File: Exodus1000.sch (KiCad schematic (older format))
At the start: 3 parts, among them J3 Conn_01x02

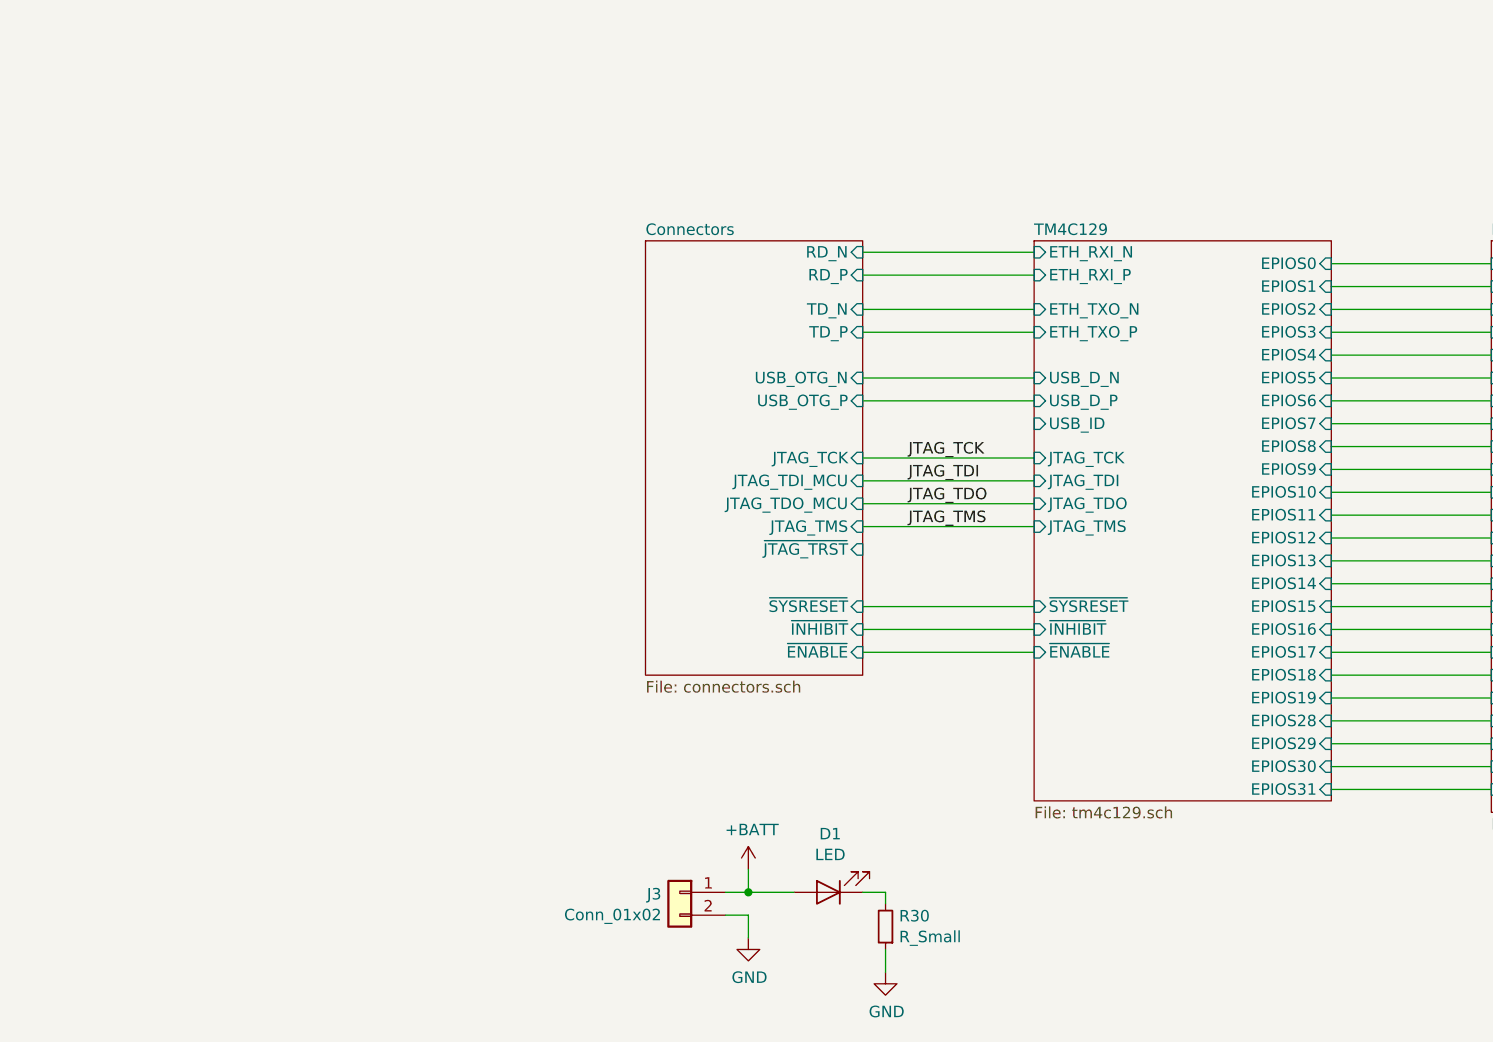
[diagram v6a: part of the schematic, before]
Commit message: layout done sans connector. It's pretty big. Likely going to need to tear some of this up.
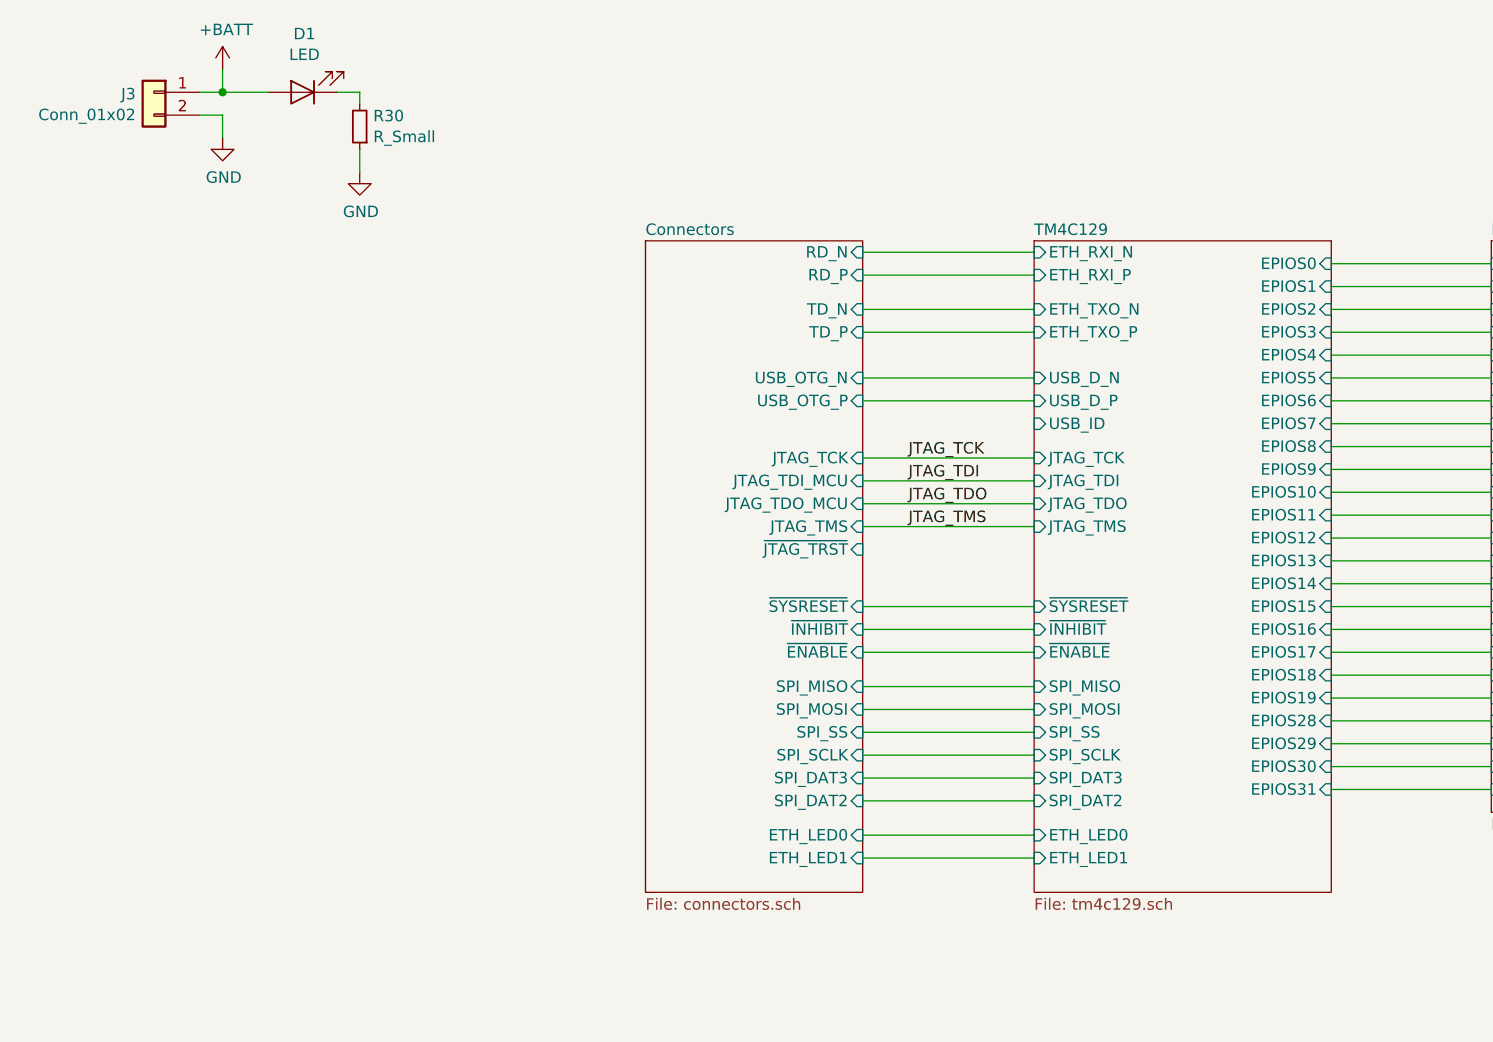
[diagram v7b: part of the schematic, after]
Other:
- moved on the sheet: D1, J3, R30
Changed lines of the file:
@@
 $EndDescr
 $Sheet
-S 5450 2050 1300 2450
+S 5450 2050 1300 2850
 U 5C80AE96
 F0 "TM4C129" 50
@@
 F38 "~INHIBIT" I L 5450 3750 50
 F39 "~SYSRESET" I L 5450 3650 50
+F40 "SPI_MISO" I L 5450 4000 50
+F41 "SPI_MOSI" I L 5450 4100 50
+F42 "SPI_SS" I L 5450 4200 50
+F43 "SPI_SCLK" I L 5450 4300 50
+F44 "SPI_DAT3" I L 5450 4400 50
+F45 "SPI_DAT2" I L 5450 4500 50
+F46 "ETH_LED0" I L 5450 4650 50
+F47 "ETH_LED1" I L 5450 4750 50
 $EndSheet
 $Sheet
-S 3750 2050 950  1900
+S 3750 2050 950  2850
 U 5C8128A2
 F0 "Connectors" 50
@@
 F14 "JTAG_TDI_MCU" I R 4700 3100 50
 F15 "JTAG_TDO_MCU" I R 4700 3200 50
+F16 "SPI_MISO" I R 4700 4000 50
+F17 "SPI_MOSI" I R 4700 4100 50
+F18 "SPI_SS" I R 4700 4200 50
+F19 "SPI_SCLK" I R 4700 4300 50
+F20 "SPI_DAT3" I R 4700 4400 50
+F21 "SPI_DAT2" I R 4700 4500 50
+F22 "ETH_LED0" I R 4700 4650 50
+F23 "ETH_LED1" I R 4700 4750 50
 $EndSheet
 Text Label 4900 3000 0    50   ~ 0
@@
 JTAG_TMS
 Wire Wire Line
-	4100 4900 4200 4900
-Wire Wire Line
-	4200 4900 4200 4800
-Wire Wire Line
-	4100 5000 4200 5000
-Wire Wire Line
-	4200 5000 4200 5100
+	1800 1400 1900 1400
+Wire Wire Line
+	1900 1400 1900 1300
+Wire Wire Line
+	1800 1500 1900 1500
+Wire Wire Line
+	1900 1500 1900 1600
 $Comp
 L power:GND #PWR0149
 U 1 1 5C8F5DB2
-P 4200 5100
-F 0 "#PWR0149" H 4200 4850 50  0001 C CNN
-F 1 "GND" H 4205 4927 50  0000 C CNN
-F 2 "" H 4200 5100 50  0001 C CNN
-F 3 "" H 4200 5100 50  0001 C CNN
-	1    4200 5100
+P 1900 1600
+F 0 "#PWR0149" H 1900 1350 50  0001 C CNN
+F 1 "GND" H 1905 1427 50  0000 C CNN
+F 2 "" H 1900 1600 50  0001 C CNN
+F 3 "" H 1900 1600 50  0001 C CNN
+	1    1900 1600
 	1    0    0    -1
 $EndComp
@@
 L power:+BATT #PWR0150
 U 1 1 5C8F5ED8
-P 4200 4800
-F 0 "#PWR0150" H 4200 4650 50  0001 C CNN
-F 1 "+BATT" H 4215 4973 50  0000 C CNN
-F 2 "" H 4200 4800 50  0001 C CNN
-F 3 "" H 4200 4800 50  0001 C CNN
-	1    4200 4800
+P 1900 1300
+F 0 "#PWR0150" H 1900 1150 50  0001 C CNN
+F 1 "+BATT" H 1915 1473 50  0000 C CNN
+F 2 "" H 1900 1300 50  0001 C CNN
+F 3 "" H 1900 1300 50  0001 C CNN
+	1    1900 1300
 	1    0    0    -1
 $EndComp
@@
 L Device:LED D1
 U 1 1 5CD7F8C0
-P 4550 4900
-F 0 "D1" H 4542 4645 50  0000 C CNN
-F 1 "LED" H 4542 4736 50  0000 C CNN
-F 2 "LED_SMD:LED_0603_1608Metric" H 4550 4900 50  0001 C CNN
-F 3 "~" H 4550 4900 50  0001 C CNN
-	1    4550 4900
+P 2250 1400
+F 0 "D1" H 2242 1145 50  0000 C CNN
+F 1 "LED" H 2242 1236 50  0000 C CNN
+F 2 "LED_SMD:LED_0603_1608Metric" H 2250 1400 50  0001 C CNN
+F 3 "~" H 2250 1400 50  0001 C CNN
+	1    2250 1400
 	-1   0    0    1
 $EndComp
 Wire Wire Line
-	4200 4900 4400 4900
-Connection ~ 4200 4900
+	1900 1400 2100 1400
+Connection ~ 1900 1400
 $Comp
 L Device:R_Small R30
 U 1 1 5CD80817
-P 4800 5050
-F 0 "R30" H 4741 5004 50  0000 R CNN
-F 1 "R_Small" H 4741 5095 50  0000 R CNN
-F 2 "Resistor_SMD:R_0603_1608Metric" H 4800 5050 50  0001 C CNN
-F 3 "~" H 4800 5050 50  0001 C CNN
-	1    4800 5050
+P 2500 1550
+F 0 "R30" H 2441 1504 50  0000 R CNN
+F 1 "R_Small" H 2441 1595 50  0000 R CNN
+F 2 "Resistor_SMD:R_0603_1608Metric" H 2500 1550 50  0001 C CNN
+F 3 "~" H 2500 1550 50  0001 C CNN
+	1    2500 1550
 	-1   0    0    1
 $EndComp
 Wire Wire Line
-	4700 4900 4800 4900
-Wire Wire Line
-	4800 4900 4800 4950
+	2400 1400 2500 1400
+Wire Wire Line
+	2500 1400 2500 1450
 $Comp
 L power:GND #PWR0184
 U 1 1 5CD81450
-P 4800 5250
-F 0 "#PWR0184" H 4800 5000 50  0001 C CNN
-F 1 "GND" H 4805 5077 50  0000 C CNN
-F 2 "" H 4800 5250 50  0001 C CNN
-F 3 "" H 4800 5250 50  0001 C CNN
-	1    4800 5250
+P 2500 1750
+F 0 "#PWR0184" H 2500 1500 50  0001 C CNN
+F 1 "GND" H 2505 1577 50  0000 C CNN
+F 2 "" H 2500 1750 50  0001 C CNN
+F 3 "" H 2500 1750 50  0001 C CNN
+	1    2500 1750
 	1    0    0    -1
 $EndComp
 Wire Wire Line
-	4800 5150 4800 5250
+	2500 1650 2500 1750
 $Comp
 L Connector_Generic:Conn_01x02 J3
 U 1 1 5C872DE6
-P 3900 4900
-F 0 "J3" H 3980 4892 50  0000 L CNN
-F 1 "Conn_01x02" H 3980 4801 50  0000 L CNN
-F 2 "Connector_PinHeader_2.54mm:PinHeader_1x02_P2.54mm_Horizontal" H 3900 4900 50  0001 C CNN
-F 3 "~" H 3900 4900 50  0001 C CNN
-	1    3900 4900
+P 1600 1400
+F 0 "J3" H 1680 1392 50  0000 L CNN
+F 1 "Conn_01x02" H 1680 1301 50  0000 L CNN
+F 2 "Connector_PinHeader_2.54mm:PinHeader_1x02_P2.54mm_Horizontal" H 1600 1400 50  0001 C CNN
+F 3 "~" H 1600 1400 50  0001 C CNN
+	1    1600 1400
 	-1   0    0    -1
 $EndComp
+Wire Wire Line
+	4700 4000 5450 4000
+Wire Wire Line
+	4700 4100 5450 4100
+Wire Wire Line
+	4700 4200 5450 4200
+Wire Wire Line
+	4700 4300 5450 4300
+Wire Wire Line
+	4700 4400 5450 4400
+Wire Wire Line
+	5450 4500 4700 4500
+Wire Wire Line
+	4700 4650 5450 4650
+Wire Wire Line
+	5450 4750 4700 4750
 $EndSCHEMATC

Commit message: this is just a mess. but I think the schematic is basically right still.
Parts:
- added J1: USB_B_Mini, Connector_USB:USB_Mini-B_Lumberg_2486_01_Horizontal, symbol Connector:USB_B_Mini
- added U1: 74LS125, Package_SO:SOIC-14_3.9x8.7mm_P1.27mm, symbol 74xx:74LS125
- J3: footprint Connector_PinHeader_2.54mm:PinHeader_1x02_P2.54mm_Horizontal -> Exodus_Connectors:Anderson_PP15_1x2_RightAngle
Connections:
- net GND: now also J1.5 (GND), J1.6 (Shield), U1.7 (GND)
- net JTAG_TDI: now also U1.11
- net JTAG_TDO: now also U1.2
- new net +3V3: U1.14 (VCC)
- new net BOARD_SENSE_1: U1.1
- new net BOARD_SENSE_2: U1.4
- new net BOARD_SENSE_3: U1.10
- new net BOARD_SENSE_4: U1.13
- new net JTAG_TDO_1: U1.3, U1.5
- new net JTAG_TDO_2: U1.6, U1.9
- new net JTAG_TDO_3: U1.12, U1.8
- new net sheet5CBA03CB/D+: J1.3 (D+)
- new net sheet5CBA03CB/D-: J1.2 (D-)
